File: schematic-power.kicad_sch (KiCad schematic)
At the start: 21 parts, among them U9 TPS62933

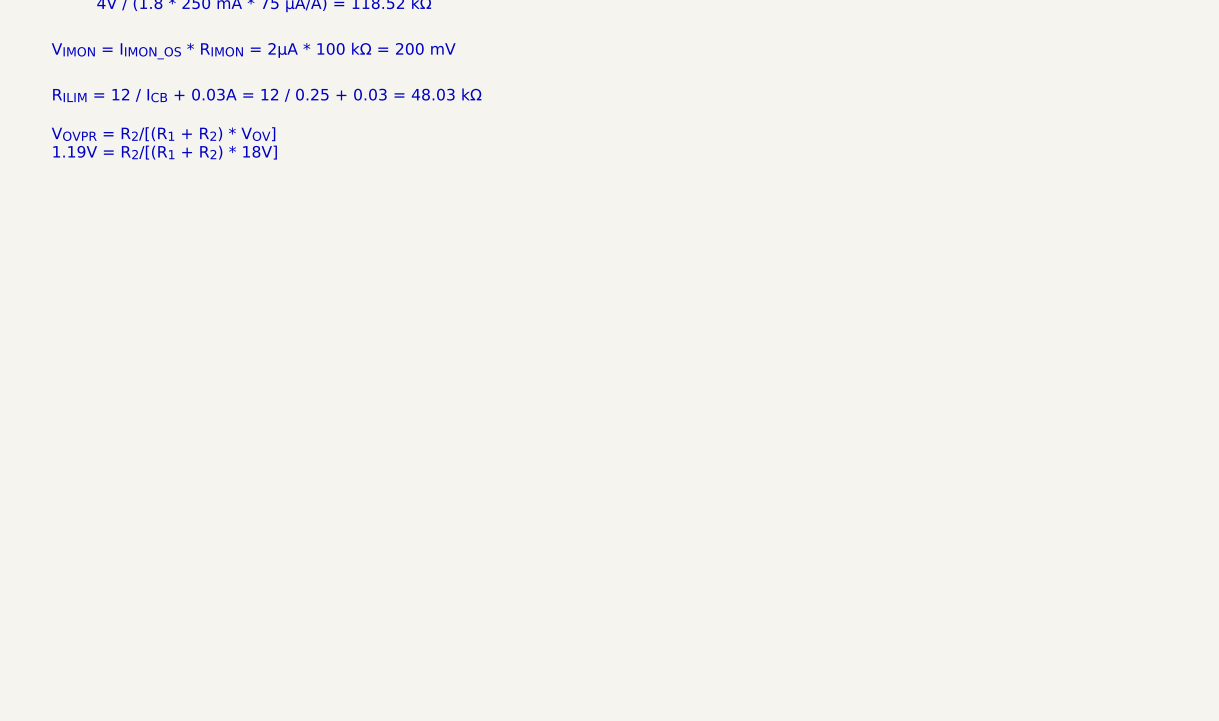
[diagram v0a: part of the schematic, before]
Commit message: Adding library and fixing errors related to the ideal diode
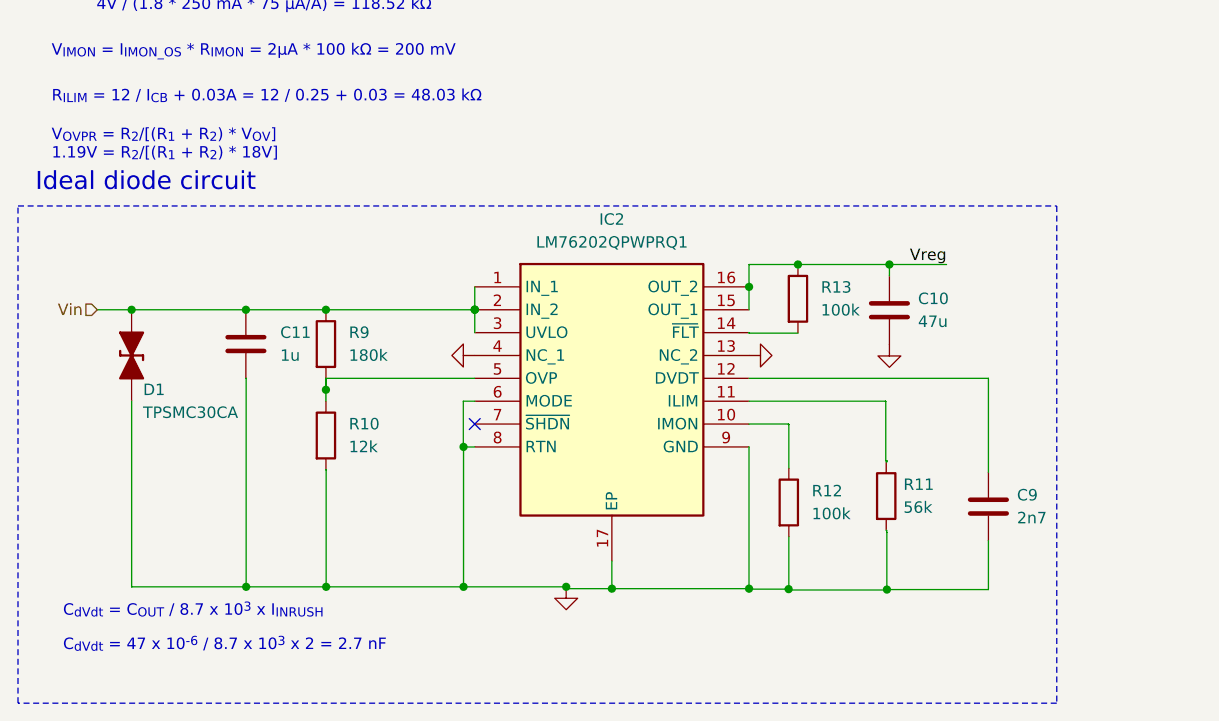
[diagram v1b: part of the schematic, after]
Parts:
- added C10: 47u, Capacitor_SMD:CP_Elec_6.3x7.7, symbol Device:C
- added C11: 1u, Capacitor_SMD:C_1206_3216Metric, symbol Device:C
- added C9: 2n7, Capacitor_SMD:C_1206_3216Metric, symbol Device:C
- added D1: TPSMC30CA, Diode_SMD:DIONM5436X244N, symbol PCM_Diode_TVS_AKL:TPSMC30CA
- added IC2: LM76202QPWPRQ1, Diode_SMD:SOP65P640X120-17N, symbol Lm7602 ideal diode:LM76202QPWPRQ1
- added R10: 12k, Resistor_SMD:R_1206_3216Metric, symbol Device:R
- added R11: 56k, Resistor_SMD:R_1206_3216Metric, symbol Device:R
- added R12, R13: 100k, Resistor_SMD:R_1206_3216Metric, symbol Device:R
- added R9: 180k, Resistor_SMD:R_1206_3216Metric, symbol Device:R
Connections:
- net GND: now also C10.2, C11.2, C9.2, D1.1 (K), IC2.13 (NC_2), IC2.17 (EP), IC2.4 (NC_1), IC2.6 (MODE), IC2.8 (RTN), IC2.9 (GND), R10.2, R11.2, R12.2
- net Vin: now also C11.1, D1.2 (A), IC2.1 (IN_1), IC2.2 (IN_2), IC2.3 (UVLO), R9.1
- net Vreg: now also C10.1, IC2.15 (OUT_1), IC2.16 (OUT_2), R13.1
- new net: IC2.10 (IMON), R12.1
- new net: IC2.5 (OVP), R10.1, R9.2
- new net: C9.1, IC2.12 (DVDT)
- new net: IC2.14 (~{FLT}), R13.2
- new net: IC2.11 (ILIM), R11.1
- no-connect marks 4 -> 5

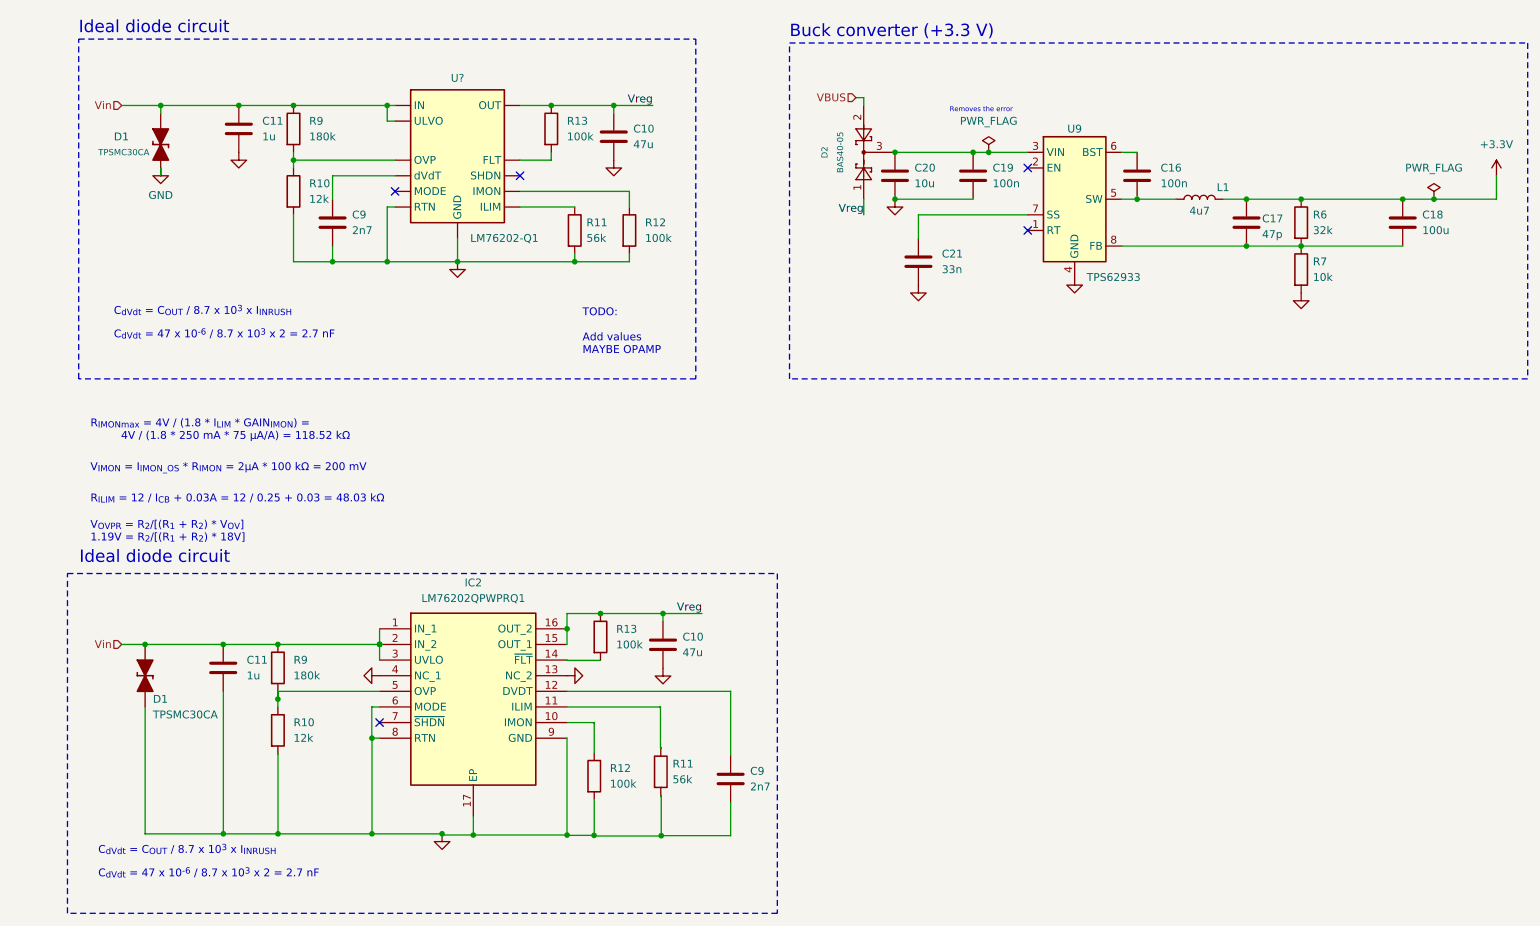
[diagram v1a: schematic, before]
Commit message: Changing placements of SolderJumper, CAN connector to 3 pins, traces 0,4
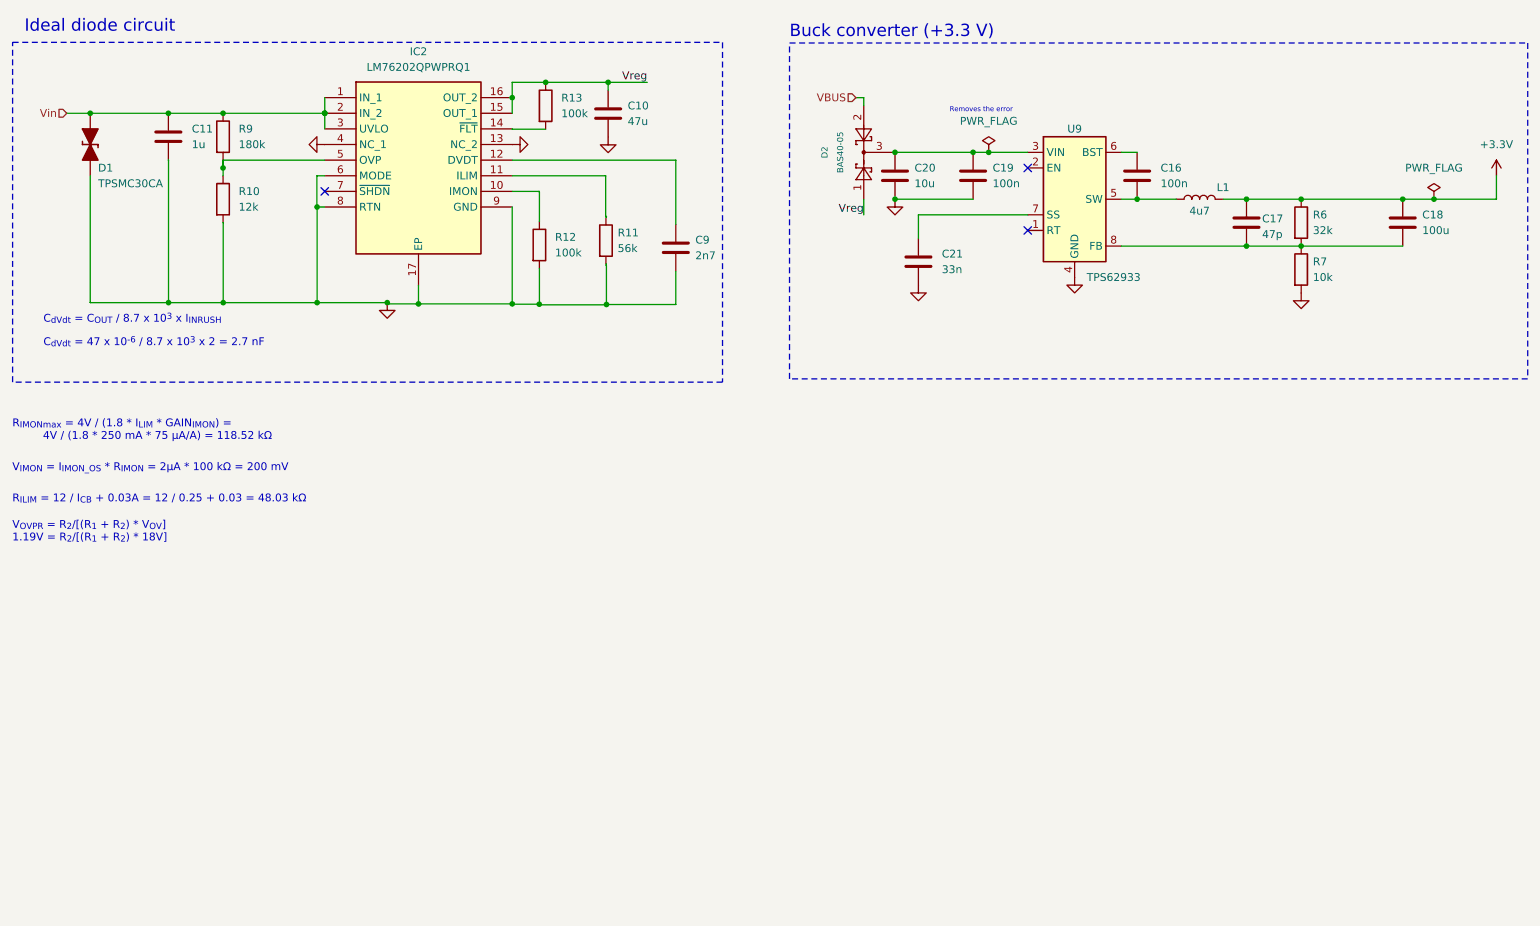
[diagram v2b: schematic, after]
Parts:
- removed C10: 47u, Capacitor_Tantalum_SMD:EEE0JA331XP, symbol Device:C
- removed C11: 1u, Capacitor_SMD:C_1206_3216Metric, symbol Device:C
- removed C9: 2n7, Capacitor_SMD:C_1206_3216Metric, symbol Device:C
- removed D1: TPSMC30CA, Diode_SMD:DIONM5436X244N, symbol PCM_Diode_TVS_AKL:TPSMC30CA
- removed R10: 12k, Resistor_SMD:R_1206_3216Metric, symbol Device:R
- removed R11: 56k, Resistor_SMD:R_1206_3216Metric, symbol Device:R
- removed R12, R13: 100k, Resistor_SMD:R_1206_3216Metric, symbol Device:R
- removed R9: 180k, Resistor_SMD:R_1206_3216Metric, symbol Device:R
- removed U?: LM76202-Q1, Diode_SMD:SOP65P640X120-17N, symbol Hydros:LM76202-Q1
- D2: footprint Package_TO_SOT_SMD:SOT-23 -> Diode_SMD:TO252__DPAK__1
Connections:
- no-connect marks 5 -> 3
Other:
- note removed: "TODO: Add values MAYBE OPAMP"
- moved on the sheet: C10, C11, C9, D1, IC2, R10, R11, R12, R13, R9

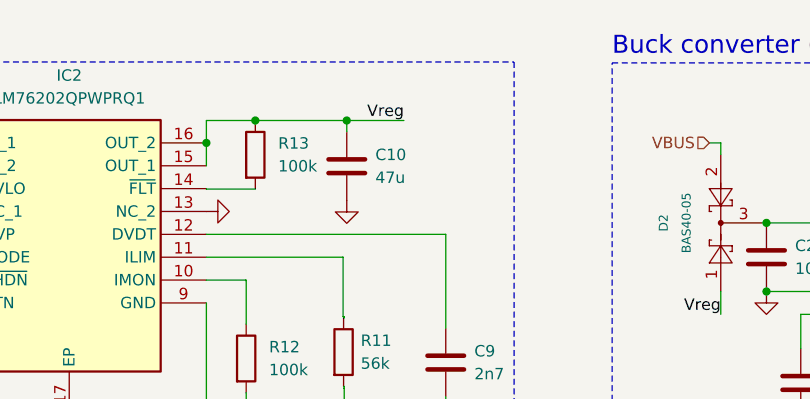
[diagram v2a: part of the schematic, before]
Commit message: Add test pins for: 3,3V, 5V, 12V and GND
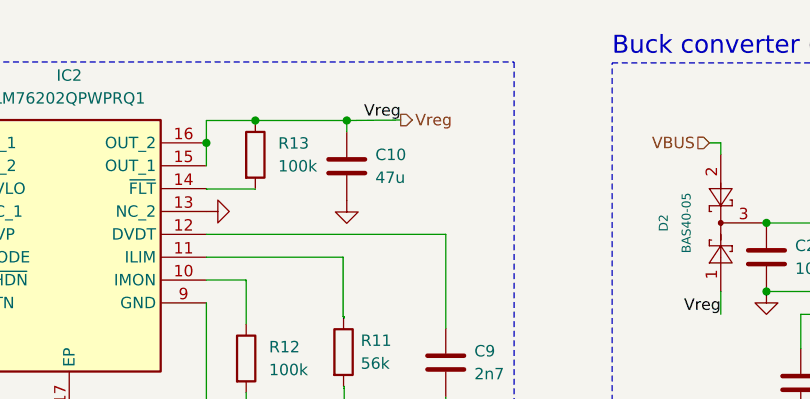
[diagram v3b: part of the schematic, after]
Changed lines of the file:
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@@
     (stroke (width 0) (type default))
   )
-  (wire (pts (xy 117.1956 57.2008) (xy 123.5456 57.2008))
+  (wire (pts (xy 117.1956 57.2008) (xy 123.19 57.15))
     (stroke (width 0) (type default))
   )
@@
     (effects (font (size 1.27 1.27)) (justify left bottom))
   )
-  (label "Vreg" (at 123.5456 57.2008 180) (fields_autoplaced)
-    (effects (font (size 1.27 1.27)) (justify right bottom))
-  )
   (label "Vreg" (at 158.75 78.74 180) (fields_autoplaced)
     (effects (font (size 1.27 1.27)) (justify right bottom))
   )
+  (label "Vreg" (at 123.19 57.15 180) (fields_autoplaced)
+    (effects (font (size 1.27 1.27)) (justify right bottom))
+  )
   (hierarchical_label "Vin" (shape input) (at 29.1846 62.23 180) (fields_autoplaced)
     (effects (font (size 1.27 1.27)) (justify right))
   )
+  (hierarchical_label "Vreg" (shape output) (at 123.19 57.15 0) (fields_autoplaced)
+    (effects (font (size 1.27 1.27)) (justify left))
+  )
   (hierarchical_label "VBUS" (shape input) (at 157.48 59.69 180) (fields_autoplaced)

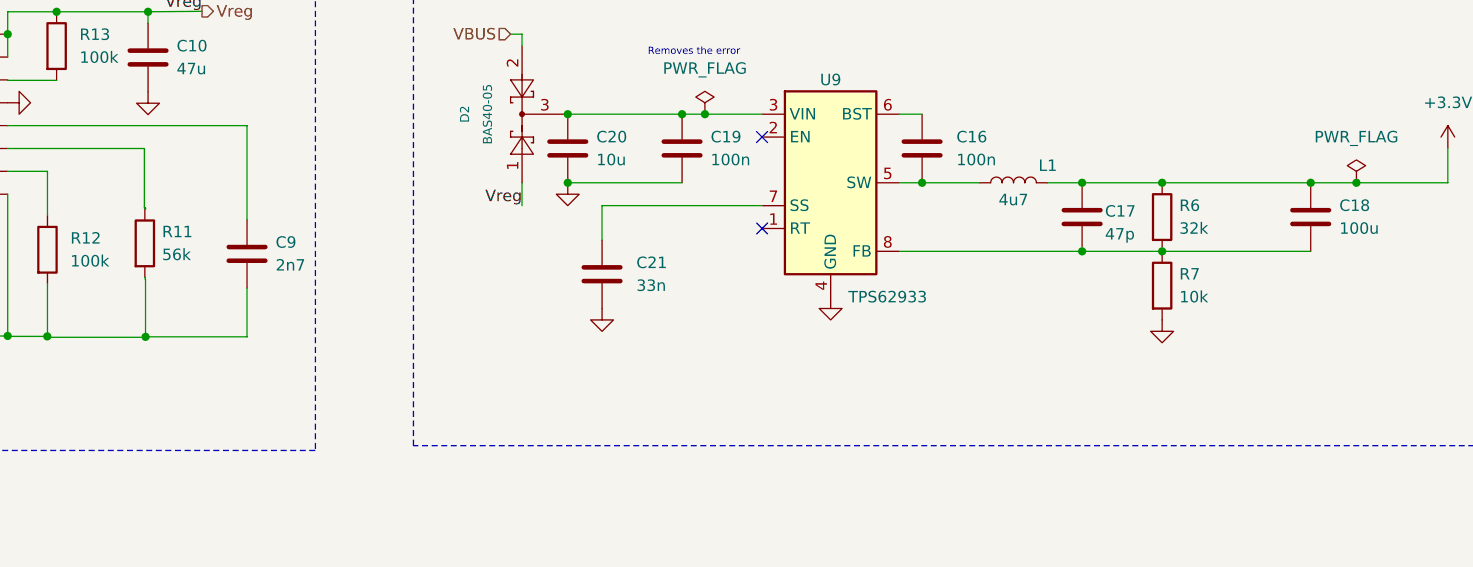
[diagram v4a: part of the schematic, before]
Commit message: Repair fedback capacitor 3.3V regulator
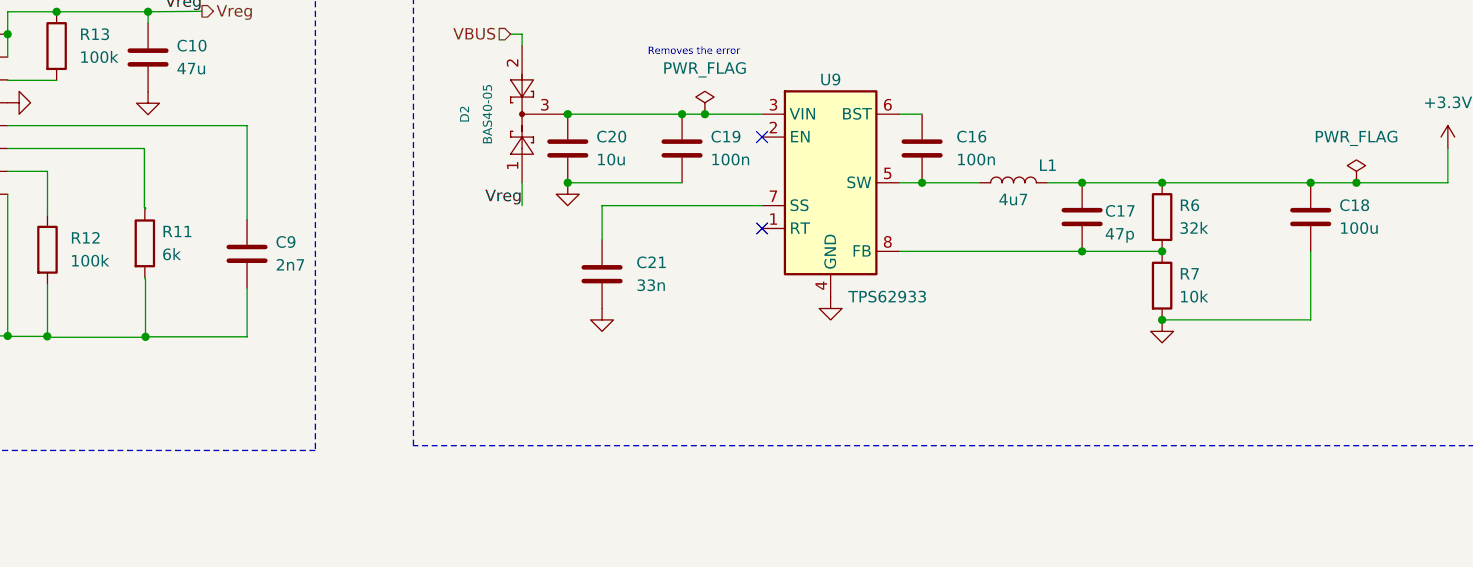
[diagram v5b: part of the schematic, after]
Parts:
- R11: value 56k -> 6k
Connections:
- net GND: now also C18.2
- net at C17.2, R6.2, R7.1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: no longer C18.2
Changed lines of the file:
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@@
+	)
+	(junction
+		(at 229.87 91.44)
+		(diameter 0)
+		(color 0 0 0 0)
 	)
 	(junction
@@
 	(wire
 		(pts
-			(xy 229.87 83.82) (xy 246.38 83.82)
-		)
-		(stroke
-			(width 0)
-			(type default)
-		)
-	)
-	(wire
-		(pts
 			(xy 116.9162 78.994) (xy 116.9162 79.121)
 		)
@@
 	(wire
 		(pts
+			(xy 246.38 91.44) (xy 229.87 91.44)
+		)
+		(stroke
+			(width 0)
+			(type default)
+		)
+	)
+	(wire
+		(pts
 			(xy 167.64 78.74) (xy 185.42 78.74)
 		)
@@
 		(pts
 			(xy 33.02 93.0148) (xy 45.72 93.0148)
+		)
+		(stroke
+			(width 0)
+			(type default)
+		)
+	)
+	(wire
+		(pts
+			(xy 246.38 83.82) (xy 246.38 91.44)
 		)
 		(stroke
@@
 			)
 		)
-		(property "Value" "56k"
+		(property "Value" "6k"
 			(at 118.745 84.2009 0)
 			(effects
